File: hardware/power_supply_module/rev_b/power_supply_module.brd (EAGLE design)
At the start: 68.1 x 66 mm, 119 parts, among them J1 MODULE_POWER, U1 TLV62130, U10 LTC2941, U11 LTC2941, U12 LTC2941, U13 LTC2941, U14 LTC2941, U15 LTC2941, U2 TLV62130, U3 TLV62130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

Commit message: used nifty rename script
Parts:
- R10, R11, R12, R13, R9: value 100 kΩ -> 10 kΩ
- R14, R15, R16, R17: value 130 kΩ -> 10 kΩ
- R18: value 240 kΩ -> 10 kΩ
- R19, R20, R21, R22: value 680 kΩ -> 10 kΩ
- R23: value 750 kΩ -> 10 kΩ
- R33, R34, R35, R36, R37: value 10 kΩ -> 100 kΩ
- R38, R39, R40, R41: value 10 kΩ -> 130 kΩ
- R42: value 10 kΩ -> 240 kΩ
- R43, R44, R45, R46: value 10 kΩ -> 680 kΩ
- R47: value 10 kΩ -> 750 kΩ
- moved R46 141.1 mm to (57.1, 12.7), turned to 270 degrees
- moved R47 135.6 mm to (18.4, 12.7), turned to 270 degrees
- moved R45 127.4 mm to (48.9, 6.35), turned to 270 degrees
- moved R41 120.0 mm to (55.9, 15.2)
- moved R44 116.4 mm to (29.2, 6.35), turned to 270 degrees
- moved R43 114.3 mm to (38.7, 6.35), turned to 270 degrees
- moved R42 112.7 mm to (17.1, 15.2)
- moved R40 106.0 mm to (47.6, 8.89)
- moved R22 101.0 mm to (0.51, -70.9), turned to 0 degrees
- moved R37 99.9 mm to (55.2, 12.7), turned to 270 degrees
- moved R39 94.0 mm to (27.9, 8.89)
- moved R38 92.5 mm to (37.5, 8.89)
- moved R23 90.4 mm to (0.51, -75.9), turned to 0 degrees
- moved R21 86.9 mm to (0.51, -65.8), turned to 0 degrees
- moved R36 85.8 mm to (47.0, 6.35), turned to 270 degrees
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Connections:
- net 3V3: now also R10.2, R11.2, R33.2, R47.2; no longer R23.2, R24.2, R25.2, R26.2
- net 5V_1: now also R12.2, R13.2, R14.2, R34.2, R43.2; no longer R11.2, R20.2, R27.2, R28.2, R29.2
- net 5V_2: now also R15.2, R16.2, R17.2, R18.2, R20.2, R44.2; no longer R10.2, R30.2, R31.2, R32.2, R33.2, R34.2
- net 5V_3: now also R24.2, R25.2, R26.2, R27.2, R28.2, R29.2, R36.2, R45.2; no longer R12.2, R21.2, R39.2, R40.2, R41.2, R42.2, R43.2, R44.2
- net 5V_4: now also R21.2, R23.2, R30.2, R31.2, R32.2; no longer R13.2, R36.2, R38.2, R45.2, R47.2
- net GND: now also R38.1, R39.1, R40.1, R41.1, R42.1; no longer R14.1, R15.1, R16.1, R17.1, R18.1
- net N$11: now also R36.1; no longer R12.1
- net N$12: now also R40.2, R45.1; no longer R16.2, R21.1
- net N$15: now also R37.1; no longer R13.1
- net N$16: now also R41.2, R46.1; no longer R17.2, R22.1
- net N$21: now also R27.1; no longer R42.1
- net N$22: now also R28.1; no longer R43.1
- net N$23: now also R21.1; no longer R36.1
- net N$24: now also R22.1; no longer R37.1
- net N$25: now also R23.1; no longer R38.1
- net N$26: now also R30.1; no longer R45.1
- net N$27: now also R31.1; no longer R46.1
- net N$3: now also R35.1; no longer R10.1
- net N$4: now also R39.2, R44.1; no longer R14.2, R19.1
- net N$43: now also R9.1; no longer R24.1
- net N$46: now also R32.1; no longer R47.1
- net N$47: now also R10.1; no longer R25.1
- net N$48: now also R29.1; no longer R44.1
- net N$49: now also R24.1; no longer R39.1
- net N$50: now also R25.1; no longer R40.1
- net N$51: now also R26.1; no longer R41.1
- net N$52: now also R15.1; no longer R30.1
- net N$53: now also R16.1; no longer R31.1
- net N$54: now also R17.1; no longer R32.1
- net N$55: now also R18.1; no longer R33.1
- net N$56: now also R19.1; no longer R34.1
- net N$57: now also R20.1; no longer R35.1
- net N$63: now also R33.1; no longer R9.1
- net N$64: now also R42.2, R47.1; no longer R18.2, R23.1
- net N$67: now also R11.1; no longer R26.1
- net N$68: now also R12.1; no longer R27.1
- net N$7: now also R34.1; no longer R11.1
- net N$70: now also R13.1; no longer R28.1
- net N$71: now also R14.1; no longer R29.1
- net N$9: now also R38.2, R43.1; no longer R15.2, R20.1

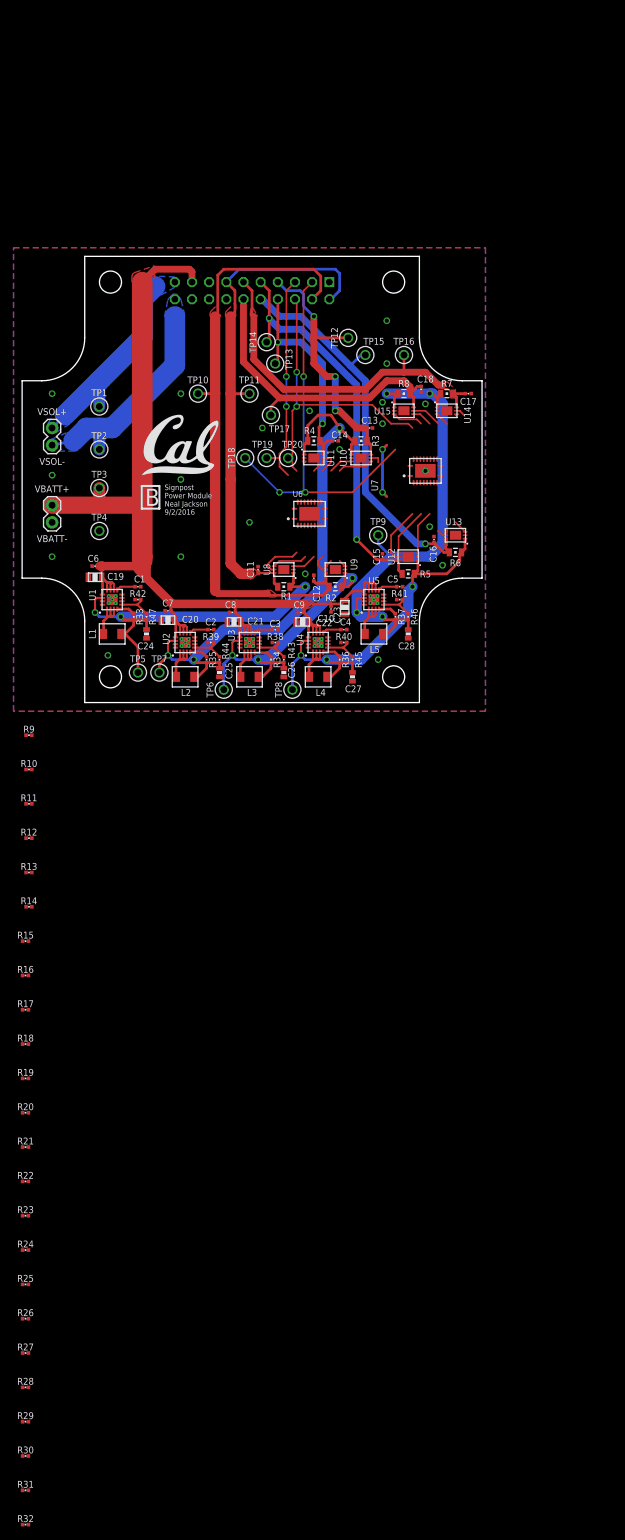
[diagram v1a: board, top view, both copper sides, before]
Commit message: routing pull-up resistors
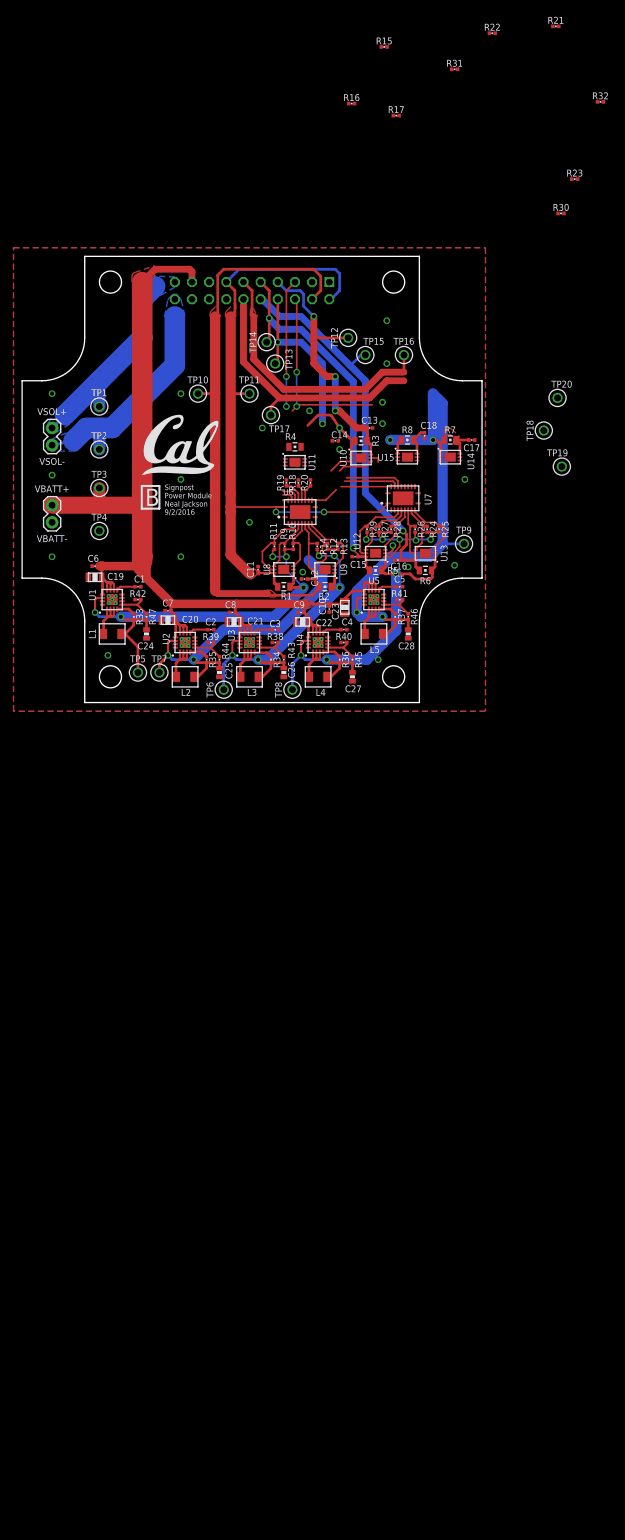
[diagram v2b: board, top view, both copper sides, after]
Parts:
- moved R32 227.1 mm to (85.6, 88.9)
- moved R31 219.7 mm to (64.0, 93.7)
- moved R30 200.2 mm to (79.8, 72.4)
- moved R21 183.5 mm to (79.0, 100.1)
- moved R22 183.4 mm to (69.6, 99.1)
- moved R23 173.6 mm to (81.8, 77.5)
- moved R17 143.3 mm to (55.4, 86.9)
- moved R15 142.6 mm to (53.6, 97.0)
- moved R29 141.4 mm to (51.1, 25.7), turned to 270 degrees
- moved R28 138.0 mm to (54.6, 25.7), turned to 270 degrees
- moved R16 137.8 mm to (48.8, 88.6)
- moved R27 132.7 mm to (52.8, 25.7), turned to 270 degrees
- moved R26 130.3 mm to (58.2, 25.7), turned to 270 degrees
- moved R25 127.4 mm to (61.7, 25.7), turned to 270 degrees
- moved R24 122.1 mm to (59.9, 25.7), turned to 270 degrees
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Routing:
- net SDA: track 58.7 -> 8.25 mm, vias 3 -> 0
- net 5V_2: track 82.8 -> 58.5 mm
- net 5V_3: track 55.9 -> 77.8 mm, vias 3 -> 8
- net VCC_BACKPLANE: track 84.0 -> 102.5 mm
- net 3V3: track 56.0 -> 66.8 mm, vias 3 -> 5
- net N$70: track 1.12 -> 9.74 mm
- net N$68: track 1.12 -> 9.51 mm
- net N$50: track 2.02 -> 9.52 mm
- net N$49: track 0.22 -> 7.67 mm
- net 5V_1: track 44.6 -> 51.7 mm, vias 3 -> 5
- net N$51: track 1.38 -> 8.04 mm
- net VCC_MOD1: track 33.1 -> 26.5 mm
- net VCC_MOD6: track 50.7 -> 44.2 mm
- net N$71: track 2.91 -> 9.14 mm
- net !INT: track 45.3 -> 39.6 mm
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
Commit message: Done routing rev B
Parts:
- removed TP10, TP11, TP12, TP13, TP14, TP15, TP16, TP17, TP18, TP19, TP2, TP20, TP3, TP4, TP5, TP6, TP7, TP8, TP9: TEST_POINT_0.040IN, headers:TESTPOINT_0.040IN
- added !INT, 3V3, 5V_1, 5V_2, 5V_3, 5V_4, BACK, GND, LINUX, MOD0, MOD1, MOD2, MOD5, MOD6, MOD7, SCL, SDA, VBATT, VSOL-: TEST_POINT_0.040IN, headers:TESTPOINT_0.040IN
- moved R21 67.5 mm to (61.7, 34.8), turned to 90 degrees
- moved R22 65.0 mm to (59.9, 34.8), turned to 90 degrees
- moved R15 64.9 mm to (46.2, 32.5), turned to 90 degrees
- moved R32 60.7 mm to (58.2, 34.8), turned to 90 degrees
- moved R31 59.7 mm to (54.6, 34.8), turned to 90 degrees
- moved R16 56.3 mm to (44.5, 32.5), turned to 90 degrees
- moved R17 54.9 mm to (48.0, 32.5), turned to 90 degrees
- moved R23 46.4 mm to (63.5, 34.8), turned to 90 degrees
- moved R30 44.3 mm to (56.4, 34.8), turned to 90 degrees
- moved R25 3.87 mm to (63.2, 22.1)
- moved C13 3.75 mm to (49.7, 37.3)
- moved R3 3.54 mm to (46.7, 37.8)
- moved C8 3.54 mm to (34.5, 12.4), turned to 0 degrees
- moved C7 3.49 mm to (24.9, 12.4), turned to 0 degrees
- moved U10 3.49 mm to (46.7, 35.6)
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- renumbered TP1 to VSOL+
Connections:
- net !INT: now also !INT.TESTPOINT; no longer TP20.TESTPOINT
- net 3V3: now also 3V3.TESTPOINT; no longer TP5.TESTPOINT
- net 5V_1: now also 5V_1.TESTPOINT; no longer TP6.TESTPOINT
- net 5V_2: now also 5V_2.TESTPOINT; no longer TP7.TESTPOINT
- net 5V_3: now also 5V_3.TESTPOINT; no longer TP8.TESTPOINT
- net 5V_4: now also 5V_4.TESTPOINT; no longer TP9.TESTPOINT
- net GND: now also GND.TESTPOINT; no longer TP4.TESTPOINT
- net SCL: now also SCL.TESTPOINT; no longer TP19.TESTPOINT
- net SDA: now also SDA.TESTPOINT; no longer TP18.TESTPOINT
- net VBATT: now also VBATT.TESTPOINT; no longer TP3.TESTPOINT
- net VCC_BACKPLANE: now also BACK.TESTPOINT; no longer TP11.TESTPOINT
- net VCC_LINUX: now also LINUX.TESTPOINT; no longer TP10.TESTPOINT
- net VCC_MOD0: now also MOD0.TESTPOINT; no longer TP12.TESTPOINT
- net VCC_MOD1: now also MOD1.TESTPOINT; no longer TP13.TESTPOINT
- net VCC_MOD2: now also MOD2.TESTPOINT; no longer TP14.TESTPOINT
- net VCC_MOD5: now also MOD5.TESTPOINT; no longer TP15.TESTPOINT
- net VCC_MOD6: now also MOD6.TESTPOINT; no longer TP16.TESTPOINT
- net VCC_MOD7: now also MOD7.TESTPOINT; no longer TP17.TESTPOINT
- net VSOL-: now also VSOL-.TESTPOINT; no longer TP2.TESTPOINT
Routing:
- net SDA: track 8.25 -> 62.9 mm, vias 0 -> 4
- net 5V_2: track 58.5 -> 98.2 mm, vias 3 -> 7
- net SCL: track 28.9 -> 60.0 mm, vias 2 -> 3
- net !INT: track 39.6 -> 57.9 mm, vias 2 -> 4
- net VBATT: track 165.1 -> 151.9 mm
- net N$25: track 0.00 -> 11.0 mm
- net N$23: track 0.00 -> 9.97 mm
- net N$54: track 1.75 -> 10.4 mm
- net N$46: track 0.00 -> 8.14 mm
- net VCC_MOD1: track 26.5 -> 34.3 mm
- net N$27: track 0.00 -> 7.10 mm
- net VCC_MOD6: track 44.2 -> 51.2 mm
- net N$24: track 0.00 -> 6.99 mm
- net N$26: track 0.00 -> 6.21 mm
- net N$57: track 2.48 -> 7.85 mm
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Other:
- board text added: "Signpost Power Module Neal Jackson 9/18/2016"
- board text removed: "Signpost Power Module Neal Jackson 9/2/2016"

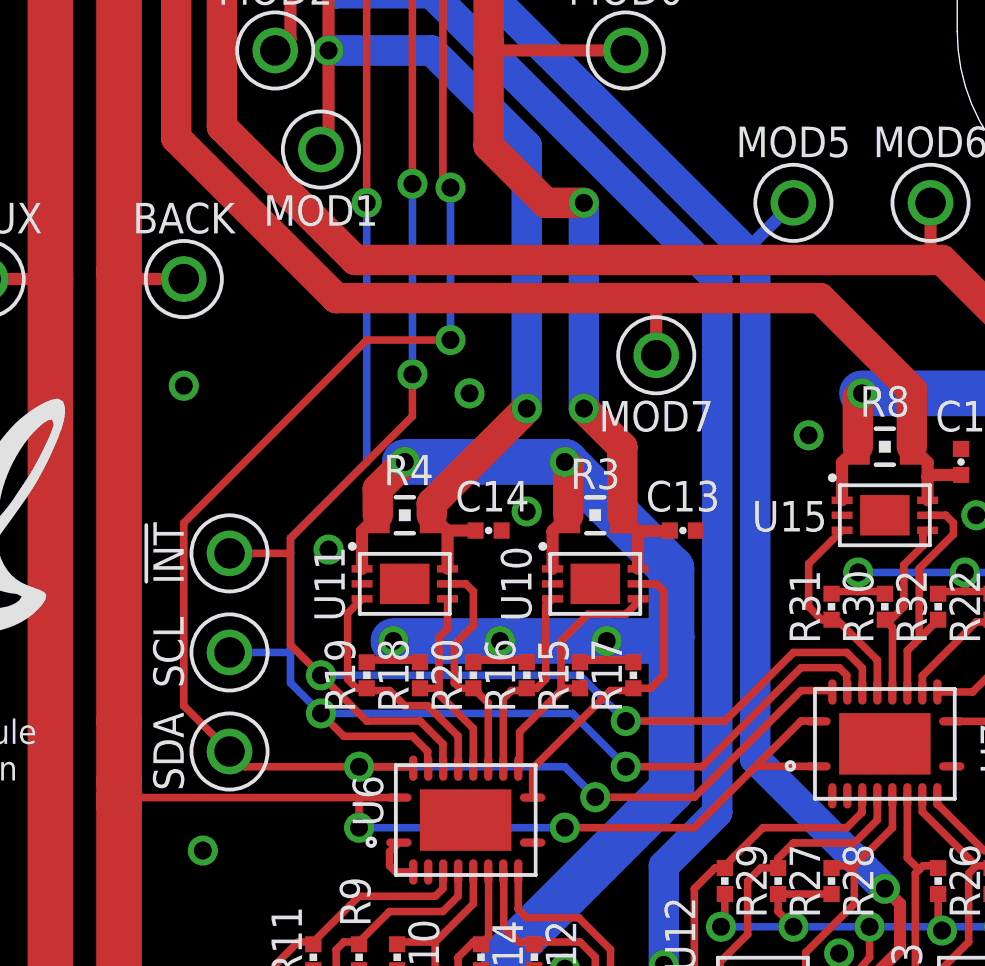
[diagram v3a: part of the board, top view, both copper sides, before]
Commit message: Moved left selector over a smidge
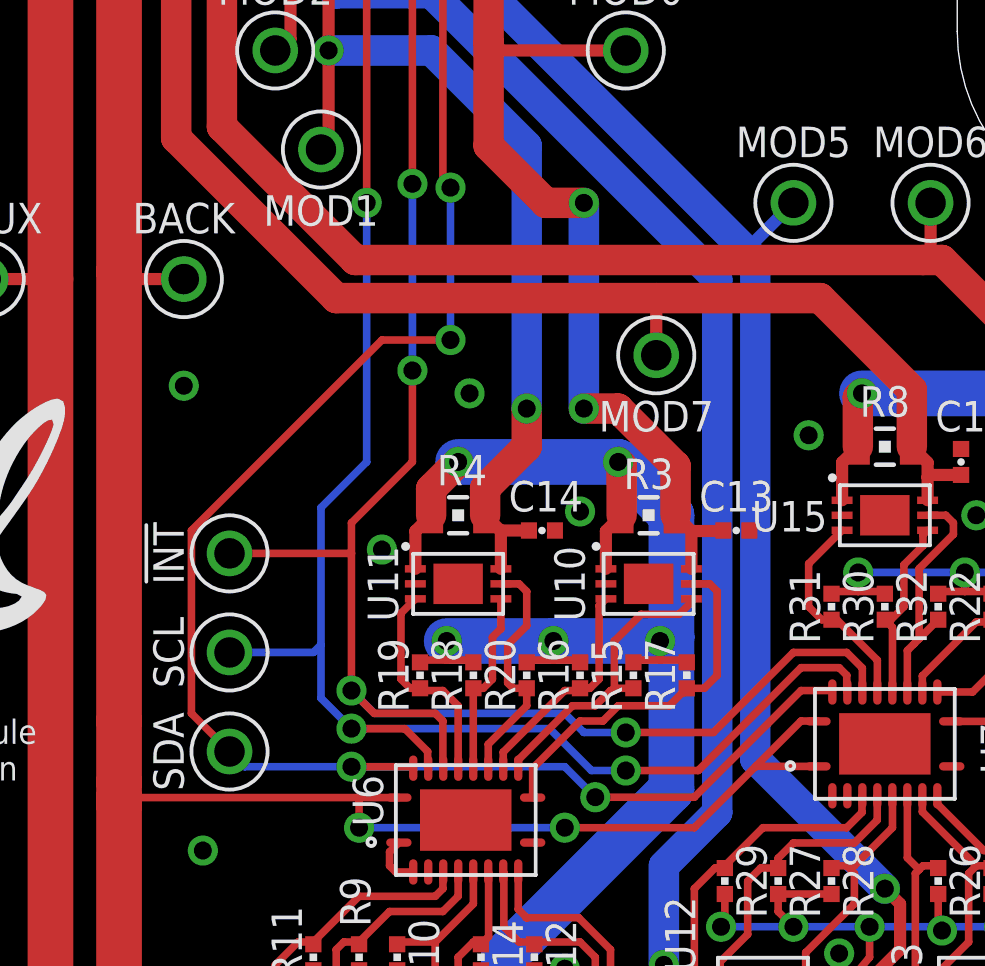
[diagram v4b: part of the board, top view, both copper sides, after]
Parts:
- moved C13 1.78 mm to (51.4, 37.3)
- moved R20 1.78 mm to (44.5, 32.5)
- moved R3 1.78 mm to (48.5, 37.8)
- moved U10 1.78 mm to (48.5, 35.6)
- moved C14 1.78 mm to (45.0, 37.3)
- moved R15 1.78 mm to (48.0, 32.5)
- moved R16 1.78 mm to (46.2, 32.5)
- moved R17 1.78 mm to (49.8, 32.5)
- moved R18 1.78 mm to (42.7, 32.5)
- moved R19 1.78 mm to (40.9, 32.5)
- moved R4 1.78 mm to (42.2, 37.8)
- moved U11 1.78 mm to (42.2, 35.6)
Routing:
- net 5V_2: track 98.2 -> 95.6 mm
- net N$54: track 10.4 -> 12.4 mm
- net VCC_MOD0: track 38.1 -> 39.5 mm
- net N$52: track 8.71 -> 9.97 mm
- net N$56: track 8.41 -> 7.23 mm
- net SCL: track 60.0 -> 58.8 mm
- net N$53: track 6.77 -> 7.51 mm
- net VCC_MOD1: track 34.3 -> 33.5 mm
- net N$55: track 6.90 -> 6.22 mm

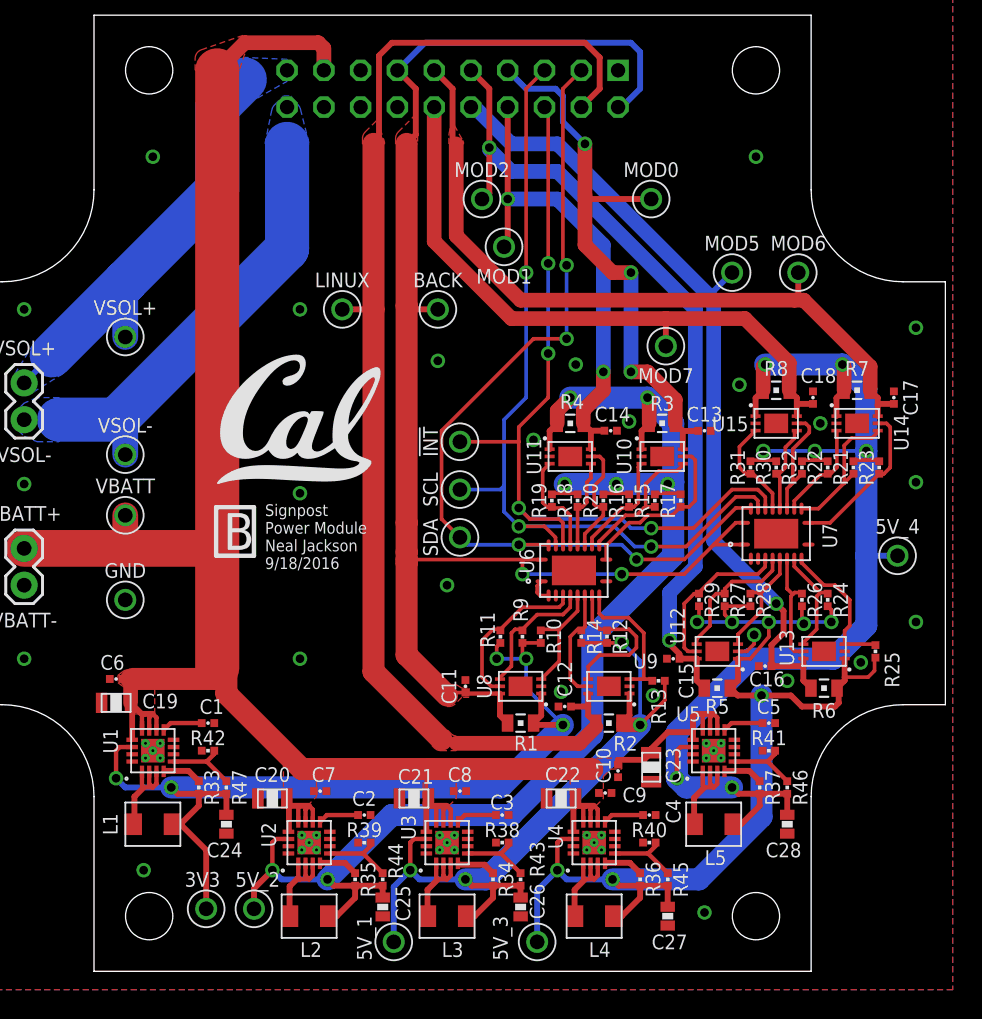
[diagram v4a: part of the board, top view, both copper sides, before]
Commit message: moved some silkscreen
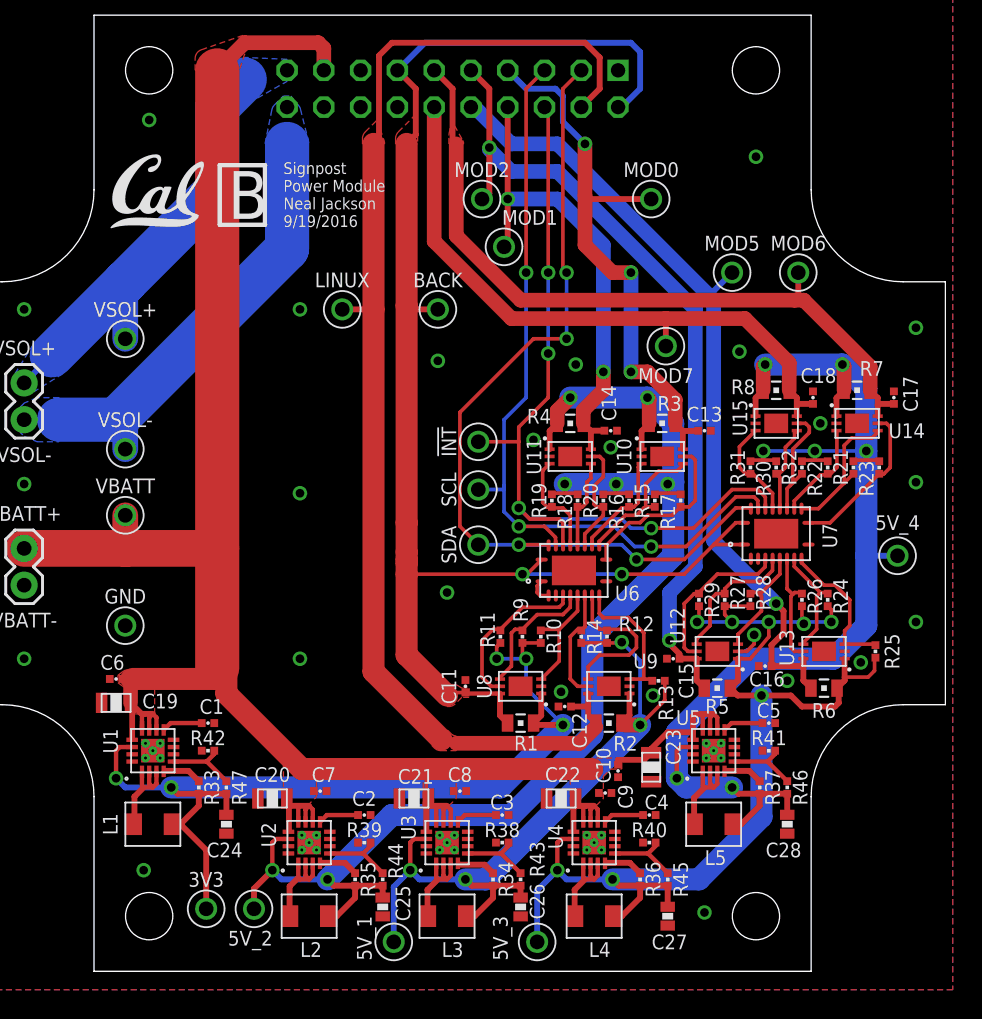
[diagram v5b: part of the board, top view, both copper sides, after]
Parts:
- U$1: device logos:UCB_CAL_350MIL -> logos:UCB_CAL_200MIL
- moved U$1 19.1 mm to (10.4, 51.3)
- moved GND 1.78 mm to (11.4, 23.9)
- moved SDA 1.37 mm to (35.8, 29.5)
- moved !INT 1.27 mm to (35.8, 36.6)
- moved SCL 1.27 mm to (35.8, 33.3)
- moved VSOL- 0.38 mm to (11.4, 36.1)
- moved VSOL+ 0.13 mm to (11.4, 43.7)
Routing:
- net SCL: track 58.8 -> 57.5 mm
- net SDA: track 62.6 -> 61.3 mm
- net !INT: track 57.5 -> 56.2 mm
- net VCC_BACKPLANE: track 105.3 -> 104.7 mm
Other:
- board text added: "Signpost Power Module Neal Jackson 9/19/2016"
- board text removed: "Signpost Power Module Neal Jackson 9/18/2016"
